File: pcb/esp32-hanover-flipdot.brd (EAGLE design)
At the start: 45.1 x 25.4 mm, 28 parts, among them J1 DC-005, J2 HANOVER, J3 FTDI, Q1 NCE3407A, Q2 S9013, U1 ESP32-PICO-D4, U2 CJA1117B-3.3-SOT89, U3 LM2576SX-5.0/NOPB

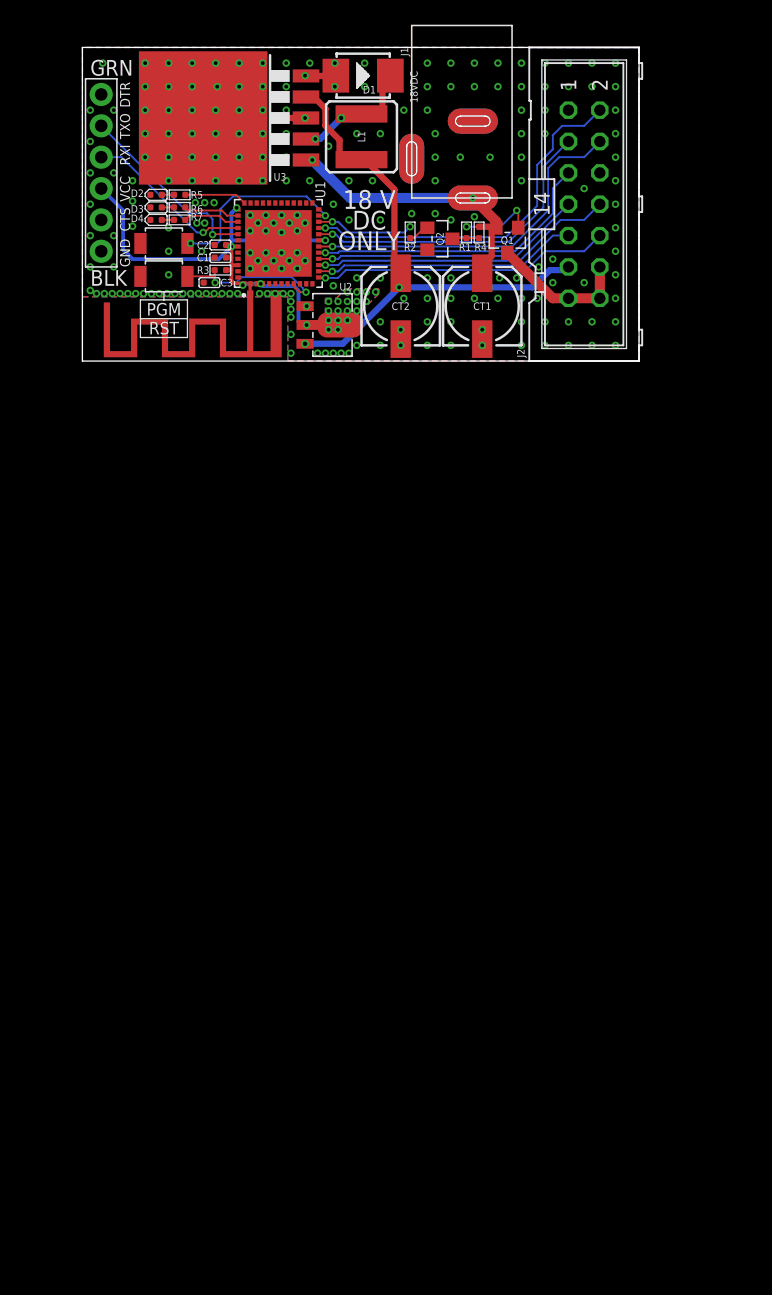
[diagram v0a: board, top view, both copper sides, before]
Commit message: pcb: Add Ethernet and PoE
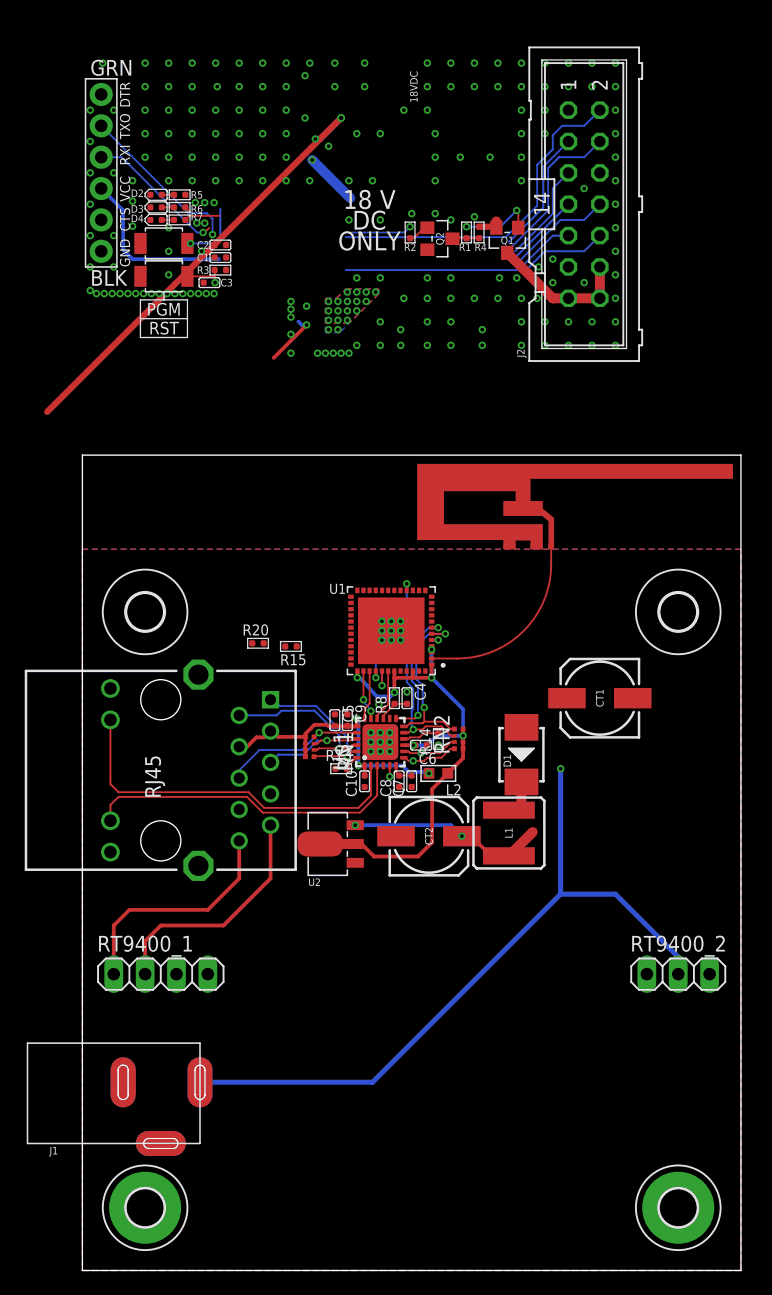
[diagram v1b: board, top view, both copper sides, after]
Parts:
- removed U3: LM2576SX-5.0/NOPB, LM2576 (1):TO263-5
- added C10, C6, C9: 10nf, OPL_Capacitor:C0402
- added C4: 4.7uf, OPL_Capacitor:C0402
- added C5: 22NF 50V, OPL_Capacitor:C0402
- added C7: 1nf, OPL_Capacitor:C0402
- added C8: 1uf, OPL_Capacitor:C0402
- added H1, H2: MOUNT-PAD-ROUND3.0, holes:3,0-PAD
- added H3, H4: MOUNT-HOLE3.0, holes:3,0
- added L2: 120OHM-500MA, OPL_Ferrite_and_Magnetic_Bead:L0603
- added R13: 12.1K, OPL_Resistor:R0402
- added R14, R8: 10K 1/16W, OPL_Resistor:R0402
- added R15, R20: 270R, OPL_Resistor:R0402
- added RN1: 49.9R, resistor-dil:YC124
- added RN2: 10K, resistor-dil:YC124
- added RT9400_1: (no value), pinhead:1X04
- added RT9400_2: (no value), pinhead:1X03
- added U$1: LAN8720, microchip-smsc-lan8720:QFN24
- added U$2: FREETRONICS-JON_HY931147C-RJ45, parts:FREETRONICS-JON_HY931147C
- E1: value ANTENNA-GROUNDEDTRACE-15.2MM -> ANTENNA-GROUNDEDTRACE-25.7MM; device SparkFun-RF:TRACE_ANTENNA_2.4GHZ_15.2MM -> SparkFun-RF:TRACE_ANTENNA_2.4GHZ_25.7MM
- moved J1 79.0 mm to (6.35, -58.4), turned to 0 degrees
- moved L1 57.6 mm to (34.5, -38.2)
- moved D1 56.5 mm to (35.6, -31.9), turned to 270 degrees
- moved CT2 43.0 mm to (28.1, -38.5), turned to 0 degrees
- moved U2 42.0 mm to (20.2, -39.1), turned to 90 degrees
- moved CT1 33.1 mm to (41.9, -27.3), turned to 180 degrees
- moved U1 32.7 mm to (25.0, -21.8), turned to 180 degrees
- moved E1 31.8 mm to (38.0, -15.2), turned to 0 degrees
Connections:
- removed net +18V: CT1.+, J1.+B, J1.+T, Q1.2, R4.2, U3.1
- new net +24V: CT1.+, J1.+B, J1.+T, Q1.2, R4.2, RT9400_2.2
- new net EMAC_CLK_OUT_180: U$1.5, U1.27
- new net EMAC_CRS_DV: RN2.2, U$1.11, U1.16
- new net EMAC_MDC: U$1.13, U1.7
- new net EMAC_MDIO: RN2.1, U$1.12, U1.6
- new net EMAC_PWR: U1.5
- new net EMAC_RXD0: RN2.3, U$1.8, U1.14
- new net EMAC_RXD1: RN2.4, U$1.7, U1.15
- new net EMAC_TXD0: U$1.17, U1.38
- new net EMAC_TXD1: U$1.18, U1.39
- new net EMAC_TX_EN: U$1.16, U1.42
- new net ETH_LED1: U$1.3, U$2.P$13
- new net ETH_LED2: U$1.2, U$2.P$12
- new net N$10: R15.2, U$2.P$14
- new net N$13: C7.2, C8.2, U$1.6
- new net N$14: R20.1, U$2.P$11
- new net N$16: C4.2, R8.1, U$1.15
- new net N$8: R14.2, U$1.10
- new net N$9: R13.2, U$1.24
- new net POE_VN: RT9400_1.1, U$2.P$10
- new net POE_VP: RT9400_1.2, U$2.P$9
- new net RXN: RN1.2, U$1.22, U$2.P$2
- new net RXP: RN1.1, U$1.23, U$2.P$1
- new net TXN: RN1.4, U$1.20, U$2.P$6
- new net TXP: RN1.3, U$1.21, U$2.P$5
- new net VDDA: C10.2, C5.2, C9.2, L2.2, RN1.5, RN1.6, RN1.7, RN1.8, U$1.1, U$1.19, U$2.P$3, U$2.P$4
- net +3V3: now also C6.2, L2.1, R20.2, R8.2, RN2.5, RN2.6, RN2.7, RN2.8, U$1.9
- net +5V: no longer U3.4
- net GND: now also C10.1, C4.1, C5.1, C6.1, C7.1, C8.1, C9.1, E1.GND2, H1.B3,0, H2.B3,0, R13.1, R14.1, R15.1, RT9400_2.1, U$1.EXP, U$2.GND1, U$2.GND2; no longer U3.3, U3.5
- net GPIO19: no longer U1.38
- net GPIO22: no longer U1.39
- net GPIO23: no longer U1.36
- net GPIO25: no longer U1.14
- net GPIO26: no longer U1.15
- net GPIO27: no longer U1.16
- net N$4: no longer U3.2
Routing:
- net +24V: track 0.00 -> 65.8 mm, vias 0 -> 2
- net N$4: track 10.2 -> 40.7 mm
- net ETH_LED2: track 0.00 -> 29.9 mm
- net +5V: track 44.3 -> 16.2 mm
- net ETH_LED1: track 0.00 -> 26.7 mm
- net VDDA: track 0.00 -> 24.2 mm, vias 0 -> 3
- net +18V: track 23.9 -> 0.00 mm, vias 2 -> 0
- net POE_VP: track 0.00 -> 19.2 mm
- net POE_VN: track 0.00 -> 18.7 mm
- net EMAC_CRS_DV: track 0.00 -> 17.4 mm, vias 0 -> 2
- net GPIO25: track 21.4 -> 4.68 mm, vias 1 -> 0
- net GPIO26: track 24.8 -> 8.37 mm, vias 1 -> 0
- net GPIO27: track 22.1 -> 5.93 mm, vias 1 -> 0
- net GPIO14: track 24.1 -> 8.14 mm, vias 1 -> 0
- net +3V3: track 44.6 -> 60.4 mm, vias 24 -> 25
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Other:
- board size 45.1 x 25.4 mm -> 53.3 x 66 mm
